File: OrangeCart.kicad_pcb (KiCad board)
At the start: 6 copper layers, 62 x 50 mm, 136 parts, among them J1 Conn_02x11_Odd_Even, J3 USB_B_Mini, J4 MicroSd, J6 JTAG, SW1 SW_Push, U1 FAN53541, U10 NCP115-2.5, U11 74AHCV17A, U12 74LVC3G17, U13 SN74LVC8T245, U14 SN74LVC8T245, U2 FAN53541, U3 LFE5U-25F-8MG285C, U4 S70KS1281, U5 74LVC06A, U6 W25Q128JVP, U7 FAN53541, U8 74LVC1G06, U9 SN74LVC8T245, X1 EXPANSION_PORT_C64_EDGE

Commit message: Increase via annular, and decrease min clearance
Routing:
- net P3.3V: track 71.6 -> 74.2 mm
- net GND: track 200.0 -> 200.5 mm, vias 147 -> 146
- net P1.1V: track 47.7 -> 47.5 mm, vias 13 -> 12
- net /sheetPower/PGOOD_P3.3V: vias 1 -> 0
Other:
- net class DDR3_CTRL_LM1.0: clearance 0.0889 -> 0.0635; via_dia 0.28 -> 0.35
- net class DDR3_DQS0_LM1.0: clearance 0.089 -> 0.0635
- net class DDR3_DQS1_LM1.0: clearance 0.089 -> 0.0635
- net class DDR_CLK_LM1.0: clearance 0.089 -> 0.0635
- net class Default: clearance 0.0889 -> 0.0635
- rule trace_clearance: 0.0889 -> 0.0635
- rule via_min_size: 0.23 -> 0.35

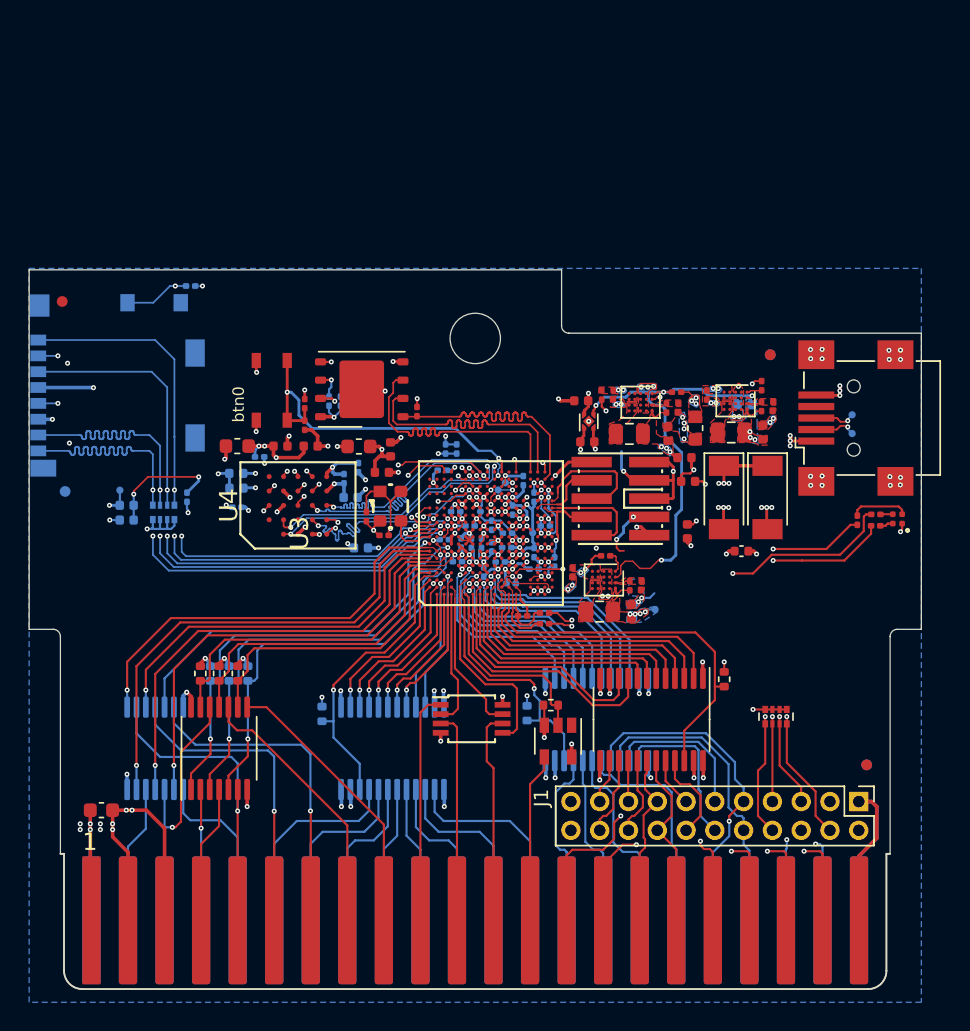
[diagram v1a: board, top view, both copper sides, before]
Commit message: Replace footprint of FPGA with 0.8mm pitch version
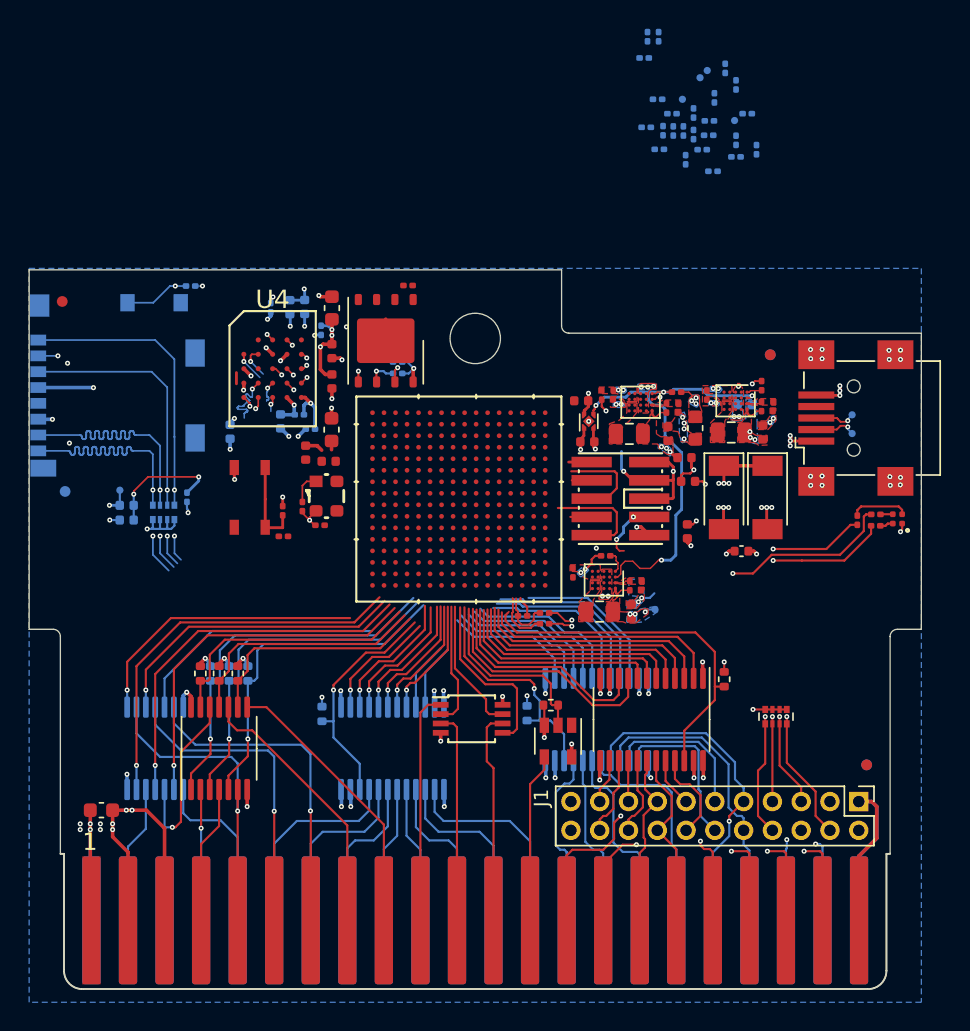
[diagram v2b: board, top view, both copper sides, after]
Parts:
- U3: value LFE5U-25F-8MG285C -> LFE5U-25F-8BG256C; footprint gkl_housings_bga:csBGA285 -> lattice:LFE5U-25F-8BG256C
- moved C49 31.9 mm to (93.0, 70.4)
- moved C51 31.9 mm to (98.1, 71.1)
- moved C57 31.9 mm to (96.6, 68.1)
- moved C59 31.9 mm to (91.9, 70.2)
- moved C64 31.9 mm to (91.7, 65.4)
- moved C66 31.9 mm to (97.4, 66.1)
- moved C67 31.9 mm to (98.9, 69.2)
- moved C68 31.9 mm to (92.8, 71.7)
- moved R27 31.9 mm to (99.5, 71.8)
- moved TP30 31.9 mm to (98.0, 69.7)
- moved C25 31.9 mm to (92.7, 63.9)
- moved C26 31.9 mm to (92.0, 63.9)
- moved C48 31.9 mm to (94.5, 70.5)
- moved C50 31.9 mm to (95.2, 69.2)
- moved C52 31.9 mm to (96.5, 73.2)
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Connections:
- U3 pad A10: SD0_CLK -> Net-(U3-PadA10)
- U3 pad A11: SD0_CD -> Net-(U3-PadA11)
- U3 pad A12: CIORD -> Net-(U3-PadA12)
- U3 pad A13: CIOWR -> Net-(U3-PadA13)
- U3 pad A15: Net-(U3-PadA15) -> NMI_OUT
- U3 pad A16: Net-(U3-PadA16) -> GND
- U3 pad A2: A15 -> SD0_DAT3
- U3 pad A3: A_DIR_H -> Net-(U3-PadA3)
- U3 pad A4: EXROM -> Net-(U3-PadA4)
- U3 pad A6: RESET_IN -> Net-(U3-PadA6)
- U3 pad A7: ROMH -> SD0_DAT2
- U3 pad A8: IO1 -> SD0_DAT1
- U3 pad A9: REF_CLK -> Net-(U3-PadA9)
- U3 pad B1: A13 -> CSPARECS
- U3 pad B10: SD0_DAT2 -> Net-(U3-PadB10)
- U3 pad B11: SD0_DAT3 -> Net-(U3-PadB11)
- U3 pad B12: CRTCCS -> Net-(U3-PadB12)
- U3 pad B15: Net-(U3-PadB15) -> RW_IN
- U3 pad B16: GND -> RW_OUT
- U3 pad B2: A14 -> CRTCCS
- U3 pad B3: GND -> SD0_DAT0
- U3 pad B4: A_~EN~_H -> Net-(U3-PadB4)
- U3 pad B6: DOTCLK -> Net-(U3-PadB6)
- U3 pad B7: RW_IN -> SD0_CLK
- U3 pad B8: IRQ_OUT -> IO1
- U3 pad C1: A11 -> CIORD
- U3 pad C10: SD0_DAT1 -> Net-(U3-PadC10)
- U3 pad C11: SD0_DAT0 -> Net-(U3-PadC11)
- U3 pad C12: CSPARECS -> Net-(U3-PadC12)
- U3 pad C15: Net-(U3-PadC15) -> PHI2
- U3 pad C16: Net-(U3-PadC16) -> RESET_OUT
- U3 pad C2: A12 -> Net-(U3-PadC2)
- U3 pad C3: A9 -> Net-(U3-PadC3)
- U3 pad C4: GAME -> Net-(U3-PadC4)
- U3 pad C6: PHI2 -> Net-(U3-PadC6)
- U3 pad C7: RW_OUT -> SD0_CD
- U3 pad C8: NMI_OUT -> REF_CLK
- U3 pad C9: SD0_CMD -> Net-(U3-PadC9)
- U3 pad D1: BA -> Net-(U3-PadD1)
- U3 pad D10: P1.1V -> Net-(U3-PadD10)
- U3 pad D11: P1.1V -> Net-(U3-PadD11)
- U3 pad D12: P3.3V -> Net-(U3-PadD12)
- U3 pad D15: Net-(U3-PadD15) -> GND
- U3 pad D16: Net-(U3-PadD16) -> DOTCLK
- U3 pad D2: IO2 -> GND
- U3 pad D3: A10 -> Net-(U3-PadD3)
- U3 pad D4: A8 -> Net-(U3-PadD4)
- U3 pad D6: RESET_OUT -> Net-(U3-PadD6)
- U3 pad D7: P3.3V -> Net-(U3-PadD7)
- U3 pad D8: P1.1V -> SD0_CMD
- U3 pad D9: P1.1V -> Net-(U3-PadD9)
- U3 pad E10: GND -> Net-(U3-PadE10)
- U3 pad E11: GND -> Net-(U3-PadE11)
- U3 pad E12: GND -> Net-(U3-PadE12)
- U3 pad E13: P2.5V -> Net-(U3-PadE13)
- U3 pad E14: GND -> Net-(U3-PadE14)
- U3 pad E5: GND -> Net-(U3-PadE5)
- U3 pad E6: P2.5V -> Net-(U3-PadE6)
- U3 pad E7: GND -> Net-(U3-PadE7)
- U3 pad E8: GND -> Net-(U3-PadE8)
- U3 pad E9: GND -> Net-(U3-PadE9)
- U3 pad F1: DMA -> Net-(U3-PadF1)
- U3 pad F10: GND -> P3.3V
- U3 pad F11: GND -> P3.3V
- U3 pad F12: GND -> Net-(U3-PadF12)
- U3 pad F13: GND -> Net-(U3-PadF13)
- U3 pad F14: GND -> Net-(U3-PadF14)
- U3 pad F15: RAM_CS# -> Net-(U3-PadF15)
- U3 pad F16: RAM_RWDS -> A8
- U3 pad F2: A_~EN~_L -> Net-(U3-PadF2)
- U3 pad F3: ROML -> Net-(U3-PadF3)
- U3 pad F4: A_DIR_L -> Net-(U3-PadF4)
- U3 pad F5: GND -> Net-(U3-PadF5)
- U3 pad F6: GND -> P3.3V
- U3 pad F7: GND -> P3.3V
- U3 pad G1: D0 -> Net-(U3-PadG1)
- U3 pad G11: GND -> P2.5V
- U3 pad G12: GND -> RESET_IN
- U3 pad G13: GND -> EXROM
- U3 pad G14: P3.3V -> A_~EN~_H
- U3 pad G15: RAM_DQ1 -> GAME
- U3 pad G16: RAM_DQ2 -> A_DIR_H
- U3 pad G2: GND -> CIOWR
- U3 pad G3: A5 -> Net-(U3-PadG3)
- U3 pad G4: A7 -> Net-(U3-PadG4)
- U3 pad G5: P3.3V -> Net-(U3-PadG5)
- U3 pad G6: GND -> P1.1V
- U3 pad G7: GND -> P1.1V
- U3 pad G9: GND -> P1.1V
- U3 pad H1: D3 -> GND
- U3 pad H11: GND -> P3.3V
- U3 pad H12: GND -> A10
- U3 pad H13: GND -> A12
- U3 pad H14: P3.3V -> A9
- U3 pad H15: P1.8V -> A14
- U3 pad H16: P1.8V -> GND
- U3 pad H2: D1 -> Net-(U3-PadH2)
- U3 pad H3: A4 -> Net-(U3-PadH3)
- U3 pad H4: A6 -> Net-(U3-PadH4)
- U3 pad H5: P3.3V -> Net-(U3-PadH5)
- U3 pad H6: GND -> P3.3V
- U3 pad H7: GND -> P3.3V
- U3 pad J1: D5 -> Net-(U3-PadJ1)
- U3 pad J11: GND -> P3.3V
- U3 pad J12: GND -> Net-(U3-PadJ12)
- U3 pad J13: GND -> Net-(U3-PadJ13)
- U3 pad J14: P1.1V -> A15
- U3 pad J15: P1.1V -> A13
- U3 pad J16: Net-(U3-PadJ16) -> IO2
- U3 pad J2: D2 -> Net-(U3-PadJ2)
- U3 pad J3: A3 -> Net-(U3-PadJ3)
- U3 pad J4: P1.1V -> Net-(U3-PadJ4)
- U3 pad J5: P1.1V -> Net-(U3-PadJ5)
- U3 pad J6: GND -> P1.8V
- U3 pad J7: GND -> P1.8V
- U3 pad K1: D7 -> Net-(U3-PadK1)
- U3 pad K11: GND -> P3.3V
- U3 pad K12: GND -> A5
- U3 pad K13: GND -> A4
- U3 pad K14: GND -> Net-(U3-PadK14)
- U3 pad K15: RAM_DQ7 -> BA
- U3 pad K16: RAM_DQ6 -> A11
- U3 pad K2: D4 -> Net-(U3-PadK2)
- U3 pad K3: A2 -> Net-(U3-PadK3)
- U3 pad K4: A1 -> RAM_RESET#
- U3 pad K5: GND -> RAM_RWDS
- U3 pad L1: D6 -> Net-(U3-PadL1)
- U3 pad L10: GND -> P1.1V
- U3 pad L11: GND -> P3.3V
- U3 pad L12: GND -> D1
- U3 pad L13: GND -> A3
- U3 pad L14: GND -> Net-(U3-PadL14)
- U3 pad L15: GND -> A7
- U3 pad L16: GND -> A6
- U3 pad L2: GND -> RAM_DQ3
- U3 pad L3: D_DIR -> Net-(U3-PadL3)
- U3 pad L4: A0 -> RAM_CS#
- U3 pad L5: GND -> RAM_DQ2
- U3 pad L6: GND -> P3.3V
- U3 pad L7: GND -> P2.5V
- U3 pad L8: GND -> P1.1V
- U3 pad L9: GND -> P1.1V
- U3 pad M1: D_~EN -> P1.8V
- U3 pad M10: GND -> JTAG_TDO
- U3 pad M11: GND -> Net-(U3-PadM11)
- U3 pad M12: GND -> USB_D-
- U3 pad M13: GND -> DMA
- U3 pad M14: P1.8V -> Net-(U3-PadM14)
- U3 pad M15: P1.1V -> ROML
- U3 pad M16: EXT_PLL+ -> A_DIR_L
- U3 pad M2: USB_D- -> P1.8V
- U3 pad M3: LED_G -> Net-(U3-PadM3)
- U3 pad M4: P1.1V -> P1.8V
- U3 pad M5: P3.3V -> GND
- U3 pad M6: GND -> Net-(U3-PadM6)
- U3 pad M7: GND -> QSPI_D2
- U3 pad M8: GND -> FPGA_RESET
- U3 pad M9: GND -> Net-(U3-PadM9)
- U3 pad N1: USB_D+ -> RAM_PSC+
- U3 pad N11: GND -> Net-(U3-PadN11)
- U3 pad N12: GND -> USB_PULLUP
- U3 pad N13: P3.3V -> A1
- U3 pad N14: P1.8V -> D3
- U3 pad N15: Net-(U3-PadN15) -> GND
- U3 pad N16: Net-(U3-PadN16) -> A_~EN~_L
- U3 pad N2: USB_PULLUP -> GND
- U3 pad N3: LED_R -> Net-(U3-PadN3)
- U3 pad N4: LED_B -> Net-(U3-PadN4)
- U3 pad N5: P3.3V -> GND
- U3 pad N6: P2.5V -> Net-(U3-PadN6)
- U3 pad N7: GND -> QSPI_D3
- U3 pad N8: GND -> SPI_CONFIG_SS
- U3 pad N9: GND -> SPI_CONFIG_SCK
- U3 pad P10: GND -> P3.3V
- U3 pad P11: P1.1V -> D_~EN
- U3 pad P12: GND -> USB_D+
- U3 pad P13: P2.5V -> LED_G
- U3 pad P14: P3.3V -> A0
- U3 pad P5: GND -> EXT_PLL-
- U3 pad P6: GND -> EXT_PLL+
- U3 pad P7: P1.1V -> Net-(U3-PadP7)
- U3 pad P8: GND -> Net-(U3-PadP8)
- U3 pad P9: P1.1V -> Net-(U3-PadP9)
- U3 pad R1: GND -> P1.8V
- U3 pad R16: Net-(U3-PadR16) -> D5
- U3 pad R2: GND -> RAM_DQ0
- U3 pad R3: GND -> RAM_CK-
- U3 pad T10: GND -> JTAG_TCK
- U3 pad T11: GND -> JTAG_TMS
- U3 pad T13: JTAG_TDI -> D6
- U3 pad T14: P3.3V -> D7
- U3 pad T15: FPGA_RESET -> LED_R
- U3 pad T2: GND -> RAM_DQ4
- U3 pad T3: GND -> RAM_DQ7
- U3 pad T4: GND -> USER_BUTTON
- U3 pad T6: GND -> Net-(U3-PadT6)
- U3 pad T7: GND -> SPI_CONFIG_MISO
- U3 pad T8: GND -> SPI_CONFIG_MOSI
- U3 pad T9: GND -> Net-(U3-PadT9)
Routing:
- net GND: track 200.5 -> 108.3 mm, vias 146 -> 92
- net P1.8V: track 55.2 -> 4.42 mm, vias 12 -> 4
- net P3.3V: track 74.2 -> 28.4 mm, vias 34 -> 20
- net SD0_CLK: track 43.1 -> 0.00 mm, vias 3 -> 0
- net P1.1V: track 47.5 -> 10.2 mm, vias 12 -> 3
- net P2.5V: track 27.2 -> 3.28 mm, vias 6 -> 1
- net SD0_CMD: track 44.0 -> 23.0 mm, vias 3 -> 2
- net SD0_DAT1: track 44.2 -> 23.8 mm, vias 3 -> 2
- net SD0_DAT0: track 44.1 -> 24.0 mm, vias 3 -> 2
- net QSPI_D2: track 19.1 -> 0.00 mm
- net SPI_CONFIG_SS: track 19.1 -> 0.00 mm
- net SPI_CONFIG_MISO: track 19.1 -> 0.00 mm
- net SD0_DAT2: track 44.0 -> 25.2 mm, vias 3 -> 2
- net USER_BUTTON: track 24.5 -> 6.24 mm, vias 2 -> 0
- net RAM_PSC+: track 17.6 -> 0.48 mm, vias 2 -> 1
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- removed copper zone on In3.Cu, net /sheetHyperRAM/RAM_VCC
- removed copper zone on In3.Cu, net /sheetHyperRAM/RAM_VCCQ
- removed copper zone on In3.Cu, net P1.8V
- removed copper zone on In3.Cu, net P2.5V
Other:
- board text removed: "Bank0"
- board text removed: "Bank1"
- board text removed: "Bank2"
- board text removed: "Bank3"
- board text removed: "Bank7"
- board text removed: "btn0"

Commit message: Mark I/O banks
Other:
- board text added: "Bank 0"
- board text added: "Bank 1"
- board text added: "Bank 2"
- board text added: "Bank 3"
- board text added: "Bank 6"
- board text added: "Bank 7"
- board text added: "Bank 8"
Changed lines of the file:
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@@
   (general
     (thickness 1.6)
-    (drawings 21)
+    (drawings 75)
     (tracks 2412)
     (zones 0)
@@
     (aux_axis_origin 80 125)
     (grid_origin 80 125)
-    (visible_elements 7FF9FF9F)
+    (visible_elements 7FF9F79F)
     (pcbplotparams
       (layerselection 0x310ff_ffffffff)
@@
       (effects (font (size 1 1) (thickness 0.15)))
     )
-    (fp_text user A (at -7.874 -6 90) (layer F.SilkS) hide
-      (effects (font (size 1 1) (thickness 0.15)))
-    )
-    (fp_text user A (at -7.874 -6 90) (layer F.Fab)
-      (effects (font (size 1 1) (thickness 0.15)))
-    )
-    (fp_text user T (at -7.874 5.999999 90) (layer F.SilkS) hide
-      (effects (font (size 1 1) (thickness 0.15)))
-    )
-    (fp_text user T (at -7.874 5.999999 90) (layer F.Fab)
-      (effects (font (size 1 1) (thickness 0.15)))
-    )
-    (fp_text user 1 (at -6 -7.874) (layer F.SilkS) hide
-      (effects (font (size 1 1) (thickness 0.15)))
-    )
-    (fp_text user 1 (at -6 -7.874) (layer F.Fab)
-      (effects (font (size 1 1) (thickness 0.15)))
-    )
-    (fp_text user 16 (at 5.999999 -8.382) (layer F.SilkS) hide
-      (effects (font (size 1 1) (thickness 0.15)))
-    )
-    (fp_text user 16 (at 5.999999 -8.382) (layer F.Fab)
-      (effects (font (size 1 1) (thickness 0.15)))
-    )
     (fp_line (start -6.9977 -2.800096) (end -7.2517 -2.800096) (layer F.SilkS) (width 0.1524))
     (fp_line (start 6.9977 -2.800096) (end 7.2517 -2.800096) (layer F.SilkS) (width 0.1524))
@@
     (fp_line (start 7.2517 -7.2517) (end 7.2517 7.2517) (layer F.CrtYd) (width 0.1524))
     (fp_line (start 7.2517 7.2517) (end -7.2517 7.2517) (layer F.CrtYd) (width 0.1524))
+    (fp_text user A (at -7.874 -6 90) (layer F.SilkS) hide
+      (effects (font (size 1 1) (thickness 0.15)))
+    )
+    (fp_text user A (at -7.874 -6 90) (layer F.Fab)
+      (effects (font (size 1 1) (thickness 0.15)))
+    )
+    (fp_text user T (at -7.874 5.999999 90) (layer F.SilkS) hide
+      (effects (font (size 1 1) (thickness 0.15)))
+    )
+    (fp_text user T (at -7.874 5.999999 90) (layer F.Fab)
+      (effects (font (size 1 1) (thickness 0.15)))
+    )
+    (fp_text user 1 (at -6 -7.874) (layer F.SilkS) hide
+      (effects (font (size 1 1) (thickness 0.15)))
+    )
+    (fp_text user 1 (at -6 -7.874) (layer F.Fab)
+      (effects (font (size 1 1) (thickness 0.15)))
+    )
+    (fp_text user 16 (at 5.999999 -8.382) (layer F.SilkS) hide
+      (effects (font (size 1 1) (thickness 0.15)))
+    )
+    (fp_text user 16 (at 5.999999 -8.382) (layer F.Fab)
+      (effects (font (size 1 1) (thickness 0.15)))
+    )
     (pad A1 smd circle (at -6 -6 90) (size 0.32512 0.32512) (layers F.Cu F.Paste F.Mask)
       (net 1 GND))
@@
     )
   )
+  (gr_line (start 85.2 102.4) (end 85.2 98.4) (layer Cmts.User) (width 0.1))
+  (gr_line (start 80.5 102.4) (end 85.2 102.4) (layer Cmts.User) (width 0.1))
+  (gr_text "Bank 6" (at 82.85 100.45) (layer Cmts.User)
+    (effects (font (size 0.5 0.5) (thickness 0.075)))
+  )
+  (gr_text "Bank 7" (at 77.05 100.95) (layer Cmts.User)
+    (effects (font (size 0.5 0.5) (thickness 0.075)))
+  )
+  (gr_line (start 79.7 98.4) (end 76.4 98.4) (layer Cmts.User) (width 0.1))
+  (gr_line (start 79.7 98.4) (end 79.7 100) (layer Cmts.User) (width 0.1))
+  (gr_line (start 81.3 98.4) (end 79.7 98.4) (layer Cmts.User) (width 0.1))
+  (gr_line (start 81.3 97.7) (end 81.3 98.4) (layer Cmts.User) (width 0.1))
+  (gr_line (start 80.5 100) (end 79.7 100) (layer Cmts.User) (width 0.1))
+  (gr_line (start 80.5 102.4) (end 80.5 100) (layer Cmts.User) (width 0.1))
+  (gr_line (start 72.5 102.35) (end 80.5 102.4) (layer Cmts.User) (width 0.1))
+  (gr_line (start 72.5 101.6) (end 72.5 102.35) (layer Cmts.User) (width 0.1))
+  (gr_text "Bank 3" (at 82.7 91.8) (layer Cmts.User)
+    (effects (font (size 0.5 0.5) (thickness 0.075)))
+  )
+  (gr_line (start 85.2 93.6) (end 85.2 95.3) (layer Cmts.User) (width 0.1))
+  (gr_line (start 81.3 94.4) (end 81.3 95.3) (layer Cmts.User) (width 0.1))
+  (gr_line (start 85.2 89.7) (end 80.4 89.7) (layer Cmts.User) (width 0.1))
+  (gr_line (start 85.2 93.6) (end 85.2 89.7) (layer Cmts.User) (width 0.1))
+  (gr_line (start 83.6 93.6) (end 85.2 93.6) (layer Cmts.User) (width 0.1))
+  (gr_line (start 83.6 94.4) (end 83.6 93.6) (layer Cmts.User) (width 0.1))
+  (gr_line (start 81.3 94.4) (end 83.6 94.4) (layer Cmts.User) (width 0.1))
+  (gr_line (start 81.3 93.6) (end 81.3 94.4) (layer Cmts.User) (width 0.1))
+  (gr_line (start 79.7 93.6) (end 81.3 93.6) (layer Cmts.User) (width 0.1))
+  (gr_text "Bank 2" (at 76.7 91) (layer Cmts.User)
+    (effects (font (size 0.5 0.5) (thickness 0.075)))
+  )
+  (gr_line (start 79.7 93.6) (end 76.4 93.6) (layer Cmts.User) (width 0.1))
+  (gr_line (start 79.7 92) (end 79.7 93.6) (layer Cmts.User) (width 0.1))
+  (gr_line (start 80.4 92) (end 79.7 92) (layer Cmts.User) (width 0.1))
+  (gr_line (start 80.4 89.7) (end 80.4 92) (layer Cmts.User) (width 0.1))
+  (gr_line (start 72.4 89.7) (end 80.4 89.7) (layer Cmts.User) (width 0.1))
+  (gr_line (start 72.4 90.5) (end 72.4 89.7) (layer Cmts.User) (width 0.1))
+  (gr_text "Bank 1" (at 74.4 94.1) (layer Cmts.User)
+    (effects (font (size 0.5 0.5) (thickness 0.075)))
+  )
+  (gr_text "Bank 0" (at 74.5 98.5) (layer Cmts.User)
+    (effects (font (size 0.5 0.5) (thickness 0.075)))
+  )
+  (gr_line (start 73.3 96.8) (end 76.4 96.8) (layer Cmts.User) (width 0.1))
+  (gr_line (start 73.3 96) (end 73.3 96.8) (layer Cmts.User) (width 0.1))
+  (gr_line (start 72.5 96) (end 73.3 96) (layer Cmts.User) (width 0.1))
+  (gr_line (start 73.3 101.6) (end 72.5 101.6) (layer Cmts.User) (width 0.1))
+  (gr_line (start 73.3 100.9) (end 73.3 101.6) (layer Cmts.User) (width 0.1))
+  (gr_line (start 74 100.9) (end 73.3 100.9) (layer Cmts.User) (width 0.1))
+  (gr_line (start 74 100) (end 74 100.9) (layer Cmts.User) (width 0.1))
+  (gr_line (start 76.4 100) (end 74 100) (layer Cmts.User) (width 0.1))
+  (gr_line (start 76.4 96.8) (end 76.4 100) (layer Cmts.User) (width 0.1))
+  (gr_line (start 76.4 92.1) (end 76.4 96.8) (layer Cmts.User) (width 0.1))
+  (gr_line (start 74.8 92.1) (end 76.4 92.1) (layer Cmts.User) (width 0.1))
+  (gr_line (start 74.1 92.1) (end 74.8 92.1) (layer Cmts.User) (width 0.1))
+  (gr_line (start 74.1 91.3) (end 74.1 92.1) (layer Cmts.User) (width 0.1))
+  (gr_line (start 73.2 91.3) (end 74.1 91.3) (layer Cmts.User) (width 0.1))
+  (gr_line (start 73.2 90.5) (end 73.2 91.3) (layer Cmts.User) (width 0.1))
+  (gr_line (start 72.4 90.5) (end 73.2 90.5) (layer Cmts.User) (width 0.1))
+  (gr_line (start 72.5 101.6) (end 72.4 90.5) (layer Cmts.User) (width 0.1))
+  (gr_text "Bank 8" (at 83.3 96.05) (layer Cmts.User)
+    (effects (font (size 0.5 0.5) (thickness 0.075)))
+  )
+  (gr_line (start 81.3 97.7) (end 81.3 95.3) (layer Cmts.User) (width 0.1))
+  (gr_line (start 83.7 97.7) (end 81.3 97.7) (layer Cmts.User) (width 0.1))
+  (gr_line (start 83.7 98.4) (end 83.7 97.7) (layer Cmts.User) (width 0.1))
+  (gr_line (start 85.2 98.4) (end 83.7 98.4) (layer Cmts.User) (width 0.1))
+  (gr_line (start 85.2 95.3) (end 85.2 98.4) (layer Cmts.User) (width 0.1))
   (gr_arc (start 86.5 84) (end 86 84) (angle -90) (layer Edge.Cuts) (width 0.05))
   (gr_line (start 86.5 84.5) (end 111 84.5) (layer Edge.Cuts) (width 0.05))

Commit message: Swap bank 2 and 6
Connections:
- U3 pad B15: RW_IN -> RAM_DQ0
- U3 pad B16: RW_OUT -> USER_BUTTON
- U3 pad C14: Net-(U3-PadC14) -> RAM_DQ1
- U3 pad C15: PHI2 -> RAM_DQ4
- U3 pad C16: RESET_OUT -> RAM_DQ3
- U3 pad D14: Net-(U3-PadD14) -> RAM_DQ2
- U3 pad D16: DOTCLK -> RAM_DQ7
- U3 pad E14: Net-(U3-PadE14) -> RAM_DQ5
- U3 pad E15: ROMH -> RAM_RWDS
- U3 pad F12: Net-(U3-PadF12) -> RAM_RESET#
- U3 pad F13: Net-(U3-PadF13) -> RAM_CS#
- U3 pad F14: Net-(U3-PadF14) -> RAM_DQ6
- U3 pad F16: A8 -> Net-(U3-PadF16)
- U3 pad G12: RESET_IN -> Net-(U3-PadG12)
- U3 pad G13: EXROM -> Net-(U3-PadG13)
- U3 pad G14: A_~EN~_H -> P1.8V
- U3 pad G15: GAME -> Net-(U3-PadG15)
- U3 pad G16: A_DIR_H -> RAM_PSC+
- U3 pad H11: P3.3V -> P1.8V
- U3 pad H12: A10 -> Net-(U3-PadH12)
- U3 pad H13: A12 -> Net-(U3-PadH13)
- U3 pad H14: A9 -> Net-(U3-PadH14)
- U3 pad H15: A14 -> RAM_PSC-
- U3 pad J11: P3.3V -> P1.8V
- U3 pad J14: A15 -> Net-(U3-PadJ14)
- U3 pad J15: A13 -> RAM_CK-
- U3 pad J16: IO2 -> RAM_CK+
- U3 pad J6: P1.8V -> P3.3V
- U3 pad J7: P1.8V -> P3.3V
- U3 pad K15: BA -> P1.8V
- U3 pad K16: A11 -> P1.8V
- U3 pad K4: RAM_RESET# -> A11
- U3 pad K5: RAM_RWDS -> IO2
- U3 pad L1: Net-(U3-PadL1) -> RW_IN
- U3 pad L2: RAM_DQ3 -> DOTCLK
- U3 pad L3: Net-(U3-PadL3) -> ROMH
- U3 pad L4: RAM_CS# -> BA
- U3 pad L5: RAM_DQ2 -> A13
- U3 pad M1: P1.8V -> RW_OUT
- U3 pad M2: P1.8V -> RESET_OUT
- U3 pad M3: Net-(U3-PadM3) -> PHI2
- U3 pad M4: P1.8V -> EXROM
- U3 pad M5: GND -> Net-(U3-PadM5)
- U3 pad N1: RAM_PSC+ -> Net-(U3-PadN1)
- U3 pad N3: Net-(U3-PadN3) -> RESET_IN
- U3 pad N5: GND -> Net-(U3-PadN5)
- U3 pad P1: RAM_DQ1 -> GAME
- U3 pad P2: RAM_PSC- -> Net-(U3-PadP2)
- U3 pad P3: Net-(U3-PadP3) -> A_DIR_H
- U3 pad P4: RAM_CK+ -> A8
- U3 pad R1: P1.8V -> A_~EN~_H
- U3 pad R2: RAM_DQ0 -> A14
- U3 pad R3: RAM_CK- -> A9
- U3 pad R4: RAM_DQ6 -> A10
- U3 pad R5: RAM_DQ5 -> Net-(U3-PadR5)
- U3 pad T2: RAM_DQ4 -> A15
- U3 pad T3: RAM_DQ7 -> A12
- U3 pad T4: USER_BUTTON -> Net-(U3-PadT4)
